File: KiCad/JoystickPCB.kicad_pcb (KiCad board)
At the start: 2 copper layers, 62 x 28 mm, 21 parts, among them J1 B4B-PH-SM4-TBT, J2 B4B-PH-SM4-TBT, U2 ADS1115IDGSR, U3 ICM-20948, U4 MIC5225-1.8YM5-TR

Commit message: Added some of the required PCB silkscreens
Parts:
- added G***: LOGO, LOGO, F.Cu at (138.6, 75.6)
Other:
- board text added: "Electrical and Computer Engineering"
- board text added: "Made in USA"
- board text added: "Still need to add assembly number and stuff"

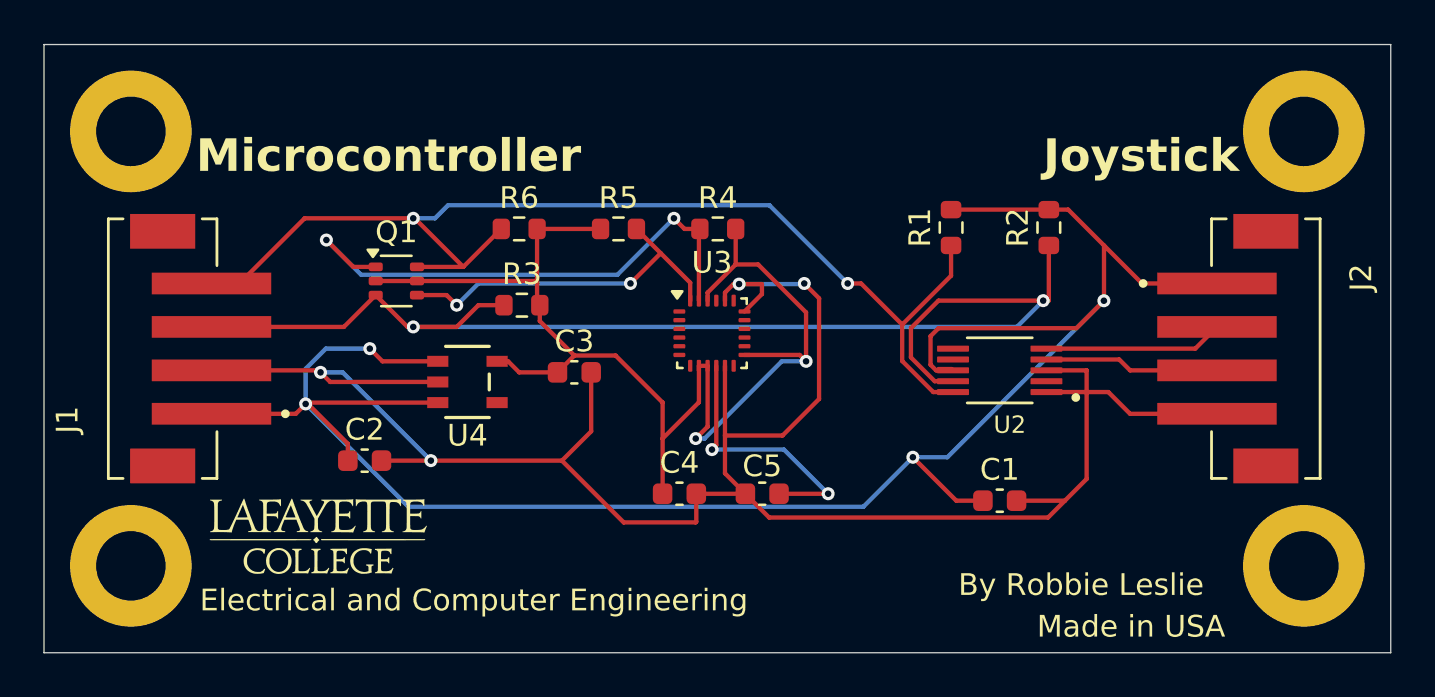
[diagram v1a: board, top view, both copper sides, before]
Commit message: Rounded corners, updated dimensions, and added comments
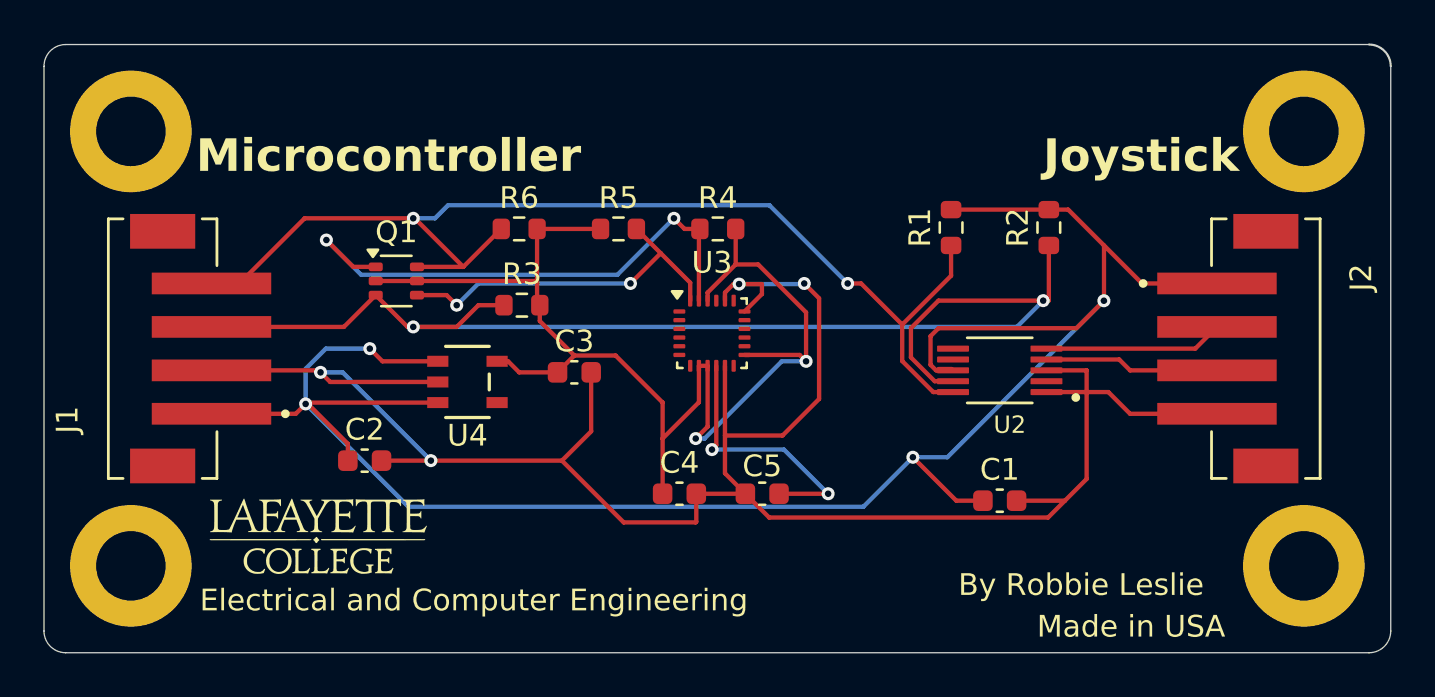
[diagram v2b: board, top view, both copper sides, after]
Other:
- outline, holes or cut-outs redrawn
- board text added: "Joystick Dimensions"
- board text added: "Might need to modify board size, although that will also proably change with the new connector"
- board text removed: "Joystick physical dimentions"
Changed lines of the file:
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@@
 		)
 	)
-	(gr_rect
-		(start 126 53)
-		(end 188 81)
-		(stroke
-			(width 0.05)
-			(type default)
-		)
-		(fill none)
+	(gr_line
+		(start 187 81)
+		(end 127 81)
+		(stroke
+			(width 0.05)
+			(type default)
+		)
+		(layer "Edge.Cuts")
+	)
+	(gr_line
+		(start 188 54)
+		(end 188 80)
+		(stroke
+			(width 0.05)
+			(type default)
+		)
+		(layer "Edge.Cuts")
+	)
+	(gr_arc
+		(start 187 53)
+		(mid 187.707107 53.292893)
+		(end 188 54)
+		(stroke
+			(width 0.1)
+			(type default)
+		)
+		(layer "Edge.Cuts")
+	)
+	(gr_arc
+		(start 188 80)
+		(mid 187.707107 80.707107)
+		(end 187 81)
+		(stroke
+			(width 0.05)
+			(type default)
+		)
+		(layer "Edge.Cuts")
+	)
+	(gr_line
+		(start 126 54)
+		(end 126 80)
+		(stroke
+			(width 0.05)
+			(type default)
+		)
+		(layer "Edge.Cuts")
+	)
+	(gr_arc
+		(start 126 54)
+		(mid 126.292893 53.292893)
+		(end 127 53)
+		(stroke
+			(width 0.05)
+			(type default)
+		)
+		(layer "Edge.Cuts")
+	)
+	(gr_arc
+		(start 127 81)
+		(mid 126.292893 80.707107)
+		(end 126 80)
+		(stroke
+			(width 0.05)
+			(type default)
+		)
+		(layer "Edge.Cuts")
+	)
+	(gr_line
+		(start 187 53)
+		(end 127 53)
+		(stroke
+			(width 0.05)
+			(type default)
+		)
 		(layer "Edge.Cuts")
 	)
@@
 		)
 	)
+	(gr_text "Joystick Dimensions"
+		(at 153 98 0)
+		(layer "Cmts.User")
+		(effects
+			(font
+				(size 1 1)
+				(thickness 0.15)
+			)
+			(justify left bottom)
+		)
+	)
 	(gr_text "Joystick ADC + IMU Breakout Board"
 		(at 186 191 0)
@@
 		)
 	)
+	(gr_text "Might need to modify board size, although that will also proably change with the new connector"
+		(at 120 100 0)
+		(layer "Cmts.User")
+		(effects
+			(font
+				(size 1 1)
+				(thickness 0.15)
+			)
+			(justify left bottom)
+		)
+	)
 	(gr_text "11/9/24"
 		(at 207 194 0)
@@
 		)
 	)
-	(gr_text "Joystick physical dimentions"
-		(at 148 96 0)
-		(layer "Cmts.User")
-		(effects
-			(font
-				(size 1 1)
-				(thickness 0.15)
-			)
-			(justify left bottom)
-		)
-	)
 	(dimension
 		(type aligned)
 		(layer "Cmts.User")
 		(pts
-			(xy 124 93) (xy 192 93)
-		)
-		(height 1)
-		(gr_text "68.0000 mm"
-			(at 158 92.2 0)
+			(xy 189 96) (xy 136 96)
+		)
+		(height 0)
+		(gr_text "53.0000 mm"
+			(at 161.876 94.1005 0)
 			(layer "Cmts.User")
 			(effects
@@
 			(thickness 0.2)
 			(arrow_length 1.27)
-			(text_position_mode 0)
+			(text_position_mode 2)
 			(extension_height 0.58642)
 			(extension_offset 0.5) keep_text_aligned)
